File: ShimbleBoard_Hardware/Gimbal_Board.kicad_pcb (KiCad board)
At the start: 2 copper layers, 85 parts, among them Q1 Q_NMOS_GDS, Q2 Q_NMOS_GDS, Q3 Q_NMOS_GDS, Q4 Q_NMOS_GDS, Q5 Q_NMOS_GDS, Q6 Q_NMOS_GDS, Q7 Q_NMOS_GDS, Q8 Q_NMOS_GDS, SW1 SW_Push, SW10 SW_SPDT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

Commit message: All Connected I Believe
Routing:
- net GND: track 179.1 -> 169.7 mm
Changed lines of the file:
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@@
     (thickness 1.6)
     (drawings 1)
-    (tracks 403)
+    (tracks 401)
     (zones 0)
     (modules 85)
@@
   (segment (start 112.903 63.627) (end 113.03 63.5) (width 0.381) (layer F.Cu) (net 2))
   (segment (start 112.903 70.612) (end 112.903 63.627) (width 0.381) (layer F.Cu) (net 2))
-  (segment (start 149.916 77.526) (end 142.24 77.526) (width 0.381) (layer F.Cu) (net 2))
-  (segment (start 151.13 78.74) (end 149.916 77.526) (width 0.381) (layer F.Cu) (net 2))
   (segment (start 142.24 77.526) (end 141.10863 77.526) (width 0.381) (layer B.Cu) (net 2))
   (segment (start 119.634 77.526) (end 119.38 77.78) (width 0.381) (layer B.Cu) (net 2))

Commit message: All Connected I Believe
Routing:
- net Net-(D9-Pad2): track 0.00 -> 1.55 mm
- net Net-(D11-Pad2): track 0.00 -> 1.55 mm
- net Net-(D10-Pad2): track 0.00 -> 1.55 mm
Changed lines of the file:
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@@
     (thickness 1.6)
     (drawings 1)
-    (tracks 401)
+    (tracks 404)
     (zones 0)
     (modules 85)
@@
   (segment (start 162.052 66.576) (end 162.842 65.786) (width 0.381) (layer F.Cu) (net 29))
   (segment (start 162.052 67.31) (end 162.052 66.576) (width 0.381) (layer F.Cu) (net 29))
+  (segment (start 113.27 90.551) (end 114.822 90.551) (width 0.381) (layer F.Cu) (net 30))
+  (segment (start 121.567 90.551) (end 120.015 90.551) (width 0.381) (layer F.Cu) (net 31))
+  (segment (start 128.298 90.551) (end 126.746 90.551) (width 0.381) (layer F.Cu) (net 85))
   (segment (start 135.029 90.551) (end 133.477 90.551) (width 0.381) (layer F.Cu) (net 86))
   (segment (start 140.208 90.551) (end 141.76 90.551) (width 0.381) (layer F.Cu) (net 87))

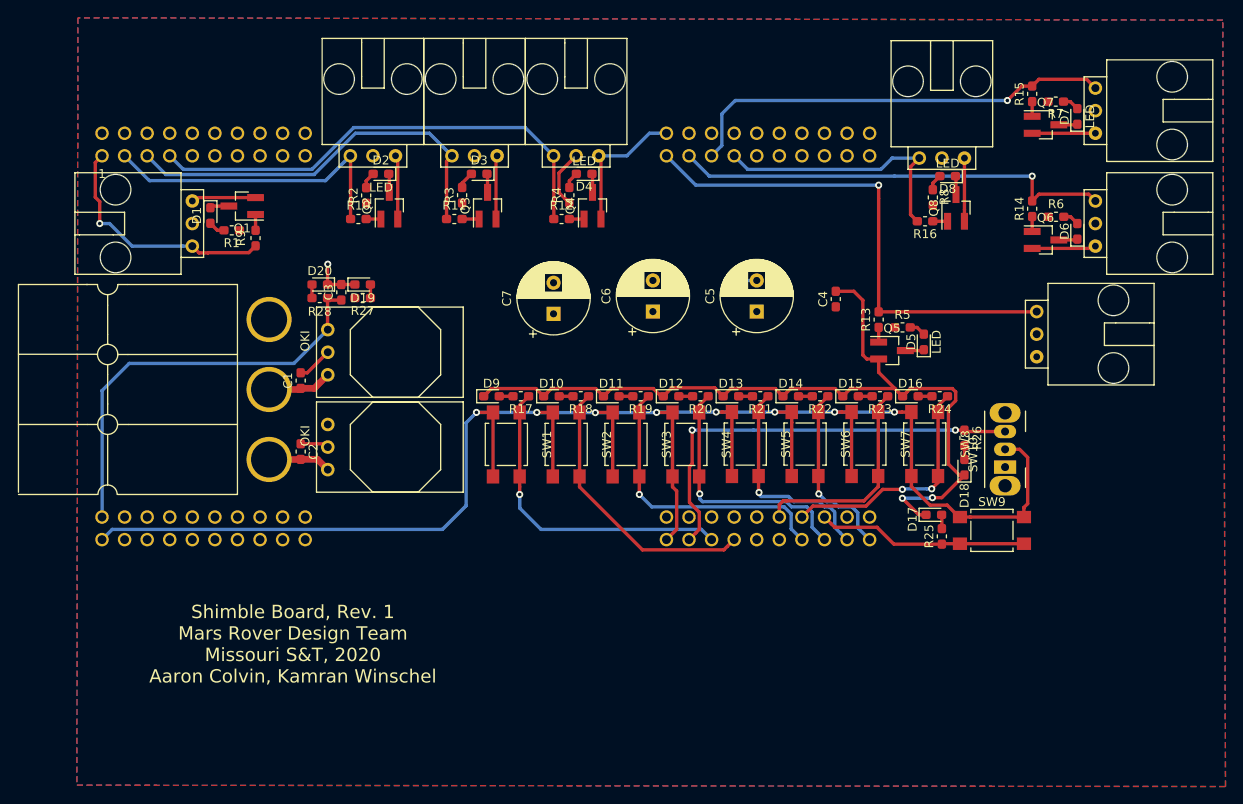
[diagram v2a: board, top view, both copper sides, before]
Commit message: Moved Labels
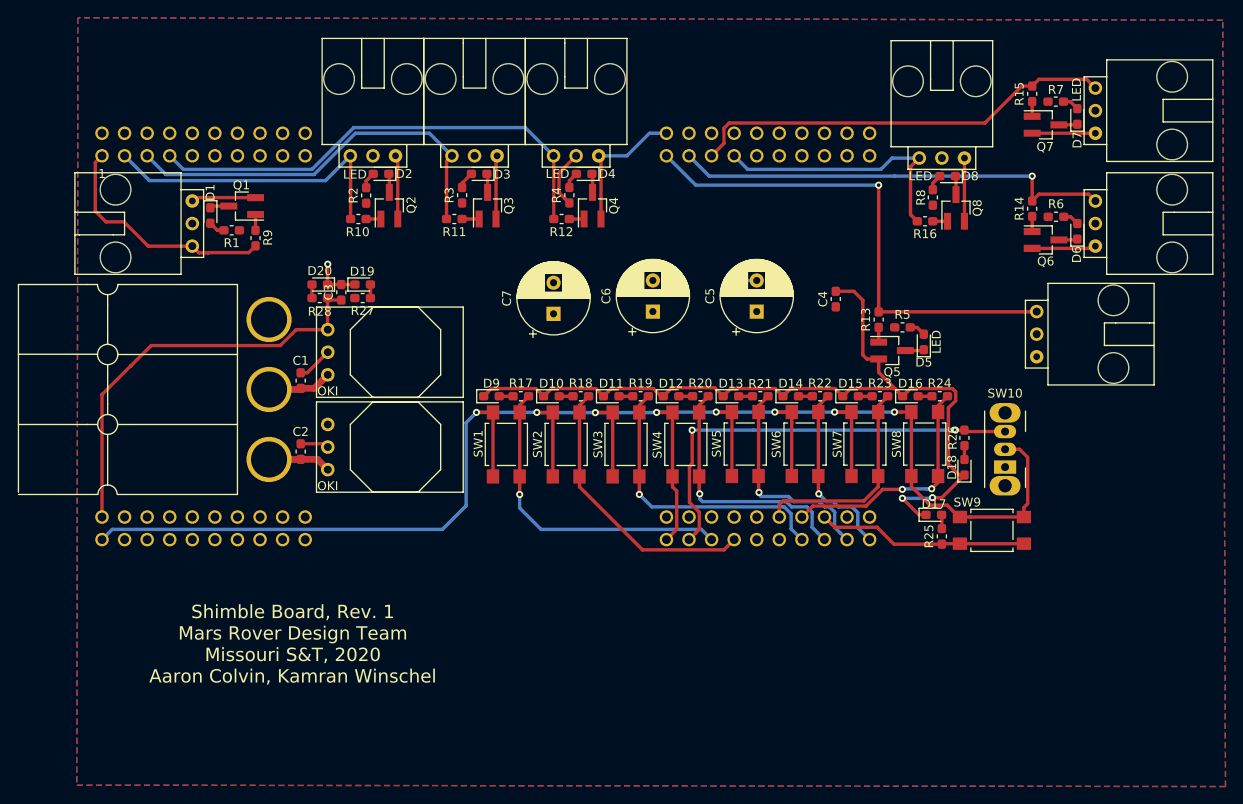
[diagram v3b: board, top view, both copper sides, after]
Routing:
- net Servo_Ctrl_7: track 49.2 -> 48.2 mm, vias 1 -> 0
- net Servo_Ctrl_1: track 27.4 -> 26.8 mm, vias 1 -> 0

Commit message: Cleaned
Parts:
- moved Q5 10.5 mm to (168.0, 85.3)
- moved R13 10.5 mm to (166.5, 81.9)
- moved D5 10.5 mm to (171.6, 84.4)
- moved R5 10.5 mm to (169.2, 82.7)
- moved C4 1.48 mm to (149.7, 79.4)
- moved C6 0.77 mm to (131.3, 81.2)
- moved C7 0.77 mm to (120.1, 81.4)
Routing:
- net GND: track 169.7 -> 167.0 mm
- net Servo_Ctrl_5: track 57.3 -> 55.3 mm, vias 1 -> 0
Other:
- board text added: "Servo Controls:"
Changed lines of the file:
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@@
   (general
     (thickness 1.6)
-    (drawings 1)
-    (tracks 403)
+    (drawings 2)
+    (tracks 409)
     (zones 0)
     (modules 85)
@@
   )
   (module Package_TO_SOT_SMD:SOT-23_Handsoldering (layer F.Cu)
-    (at 157.456 85.41)
+    (at 167.997 85.3465)
     (descr "SOT-23, Handsoldering")
     (tags SOT-23)
@@
   )
   (module Capacitor_THT:CP_Radial_D8.0mm_P3.50mm (layer F.Cu)
-    (at 130.556 81.026 90)
+    (at 131.318 81.153 90)
     (descr "CP, Radial series, Radial, pin pitch=3.50mm, , diameter=8mm, Electrolytic Capacitor")
     (tags "CP Radial series Radial pin pitch 3.50mm  diameter 8mm Electrolytic Capacitor")
@@
   )
   (module Capacitor_SMD:C_0603_1608Metric_Pad1.05x0.95mm_HandSolder (layer F.Cu)
-    (at 151.13 79.615 90)
+    (at 149.6695 79.361 90)
     (descr "Capacitor SMD 0603 (1608 Metric), square (rectangular) end terminal, IPC_7351 nominal with elongated pad for handsoldering. (Body size source: http://www.tortai-tech.com/upload/download/2011102023233369053.pdf), generated with kicad-footprint-generator")
     (tags "capacitor handsolder")
@@
   )
   (module Diode_SMD:D_0603_1608Metric_Pad1.05x0.95mm_HandSolder (layer F.Cu)
-    (at 161.036 84.441 90)
+    (at 171.577 84.3775 90)
     (descr "Diode SMD 0603 (1608 Metric), square (rectangular) end terminal, IPC_7351 nominal, (Body size source: http://www.tortai-tech.com/upload/download/2011102023233369053.pdf), generated with kicad-footprint-generator")
     (tags "diode handsolder")
     (attr smd)
-    (fp_text reference D5 (at -2.3 0 180) (layer F.SilkS)
+    (fp_text reference D5 (at -2.5794 -0.0254 270) (layer F.SilkS)
       (effects (font (size 1 1) (thickness 0.15)))
     )
-    (fp_text value LED (at 0 1.43 90) (layer F.SilkS)
+    (fp_text value LED (at 2.9705 0.0635 90) (layer F.SilkS)
       (effects (font (size 1 1) (thickness 0.15)))
     )
@@
   )
   (module Resistor_SMD:R_0603_1608Metric_Pad1.05x0.95mm_HandSolder (layer F.Cu)
-    (at 158.637 82.804)
+    (at 169.178 82.7405)
     (descr "Resistor SMD 0603 (1608 Metric), square (rectangular) end terminal, IPC_7351 nominal with elongated pad for handsoldering. (Body size source: http://www.tortai-tech.com/upload/download/2011102023233369053.pdf), generated with kicad-footprint-generator")
     (tags "resistor handsolder")
@@
   )
   (module Resistor_SMD:R_0603_1608Metric_Pad1.05x0.95mm_HandSolder (layer F.Cu)
-    (at 155.956 81.929 90)
+    (at 166.497 81.8655 90)
     (descr "Resistor SMD 0603 (1608 Metric), square (rectangular) end terminal, IPC_7351 nominal with elongated pad for handsoldering. (Body size source: http://www.tortai-tech.com/upload/download/2011102023233369053.pdf), generated with kicad-footprint-generator")
     (tags "resistor handsolder")
@@
   )
   (module Capacitor_THT:CP_Radial_D8.0mm_P3.50mm (layer F.Cu)
-    (at 119.38 81.28 90)
+    (at 120.142 81.407 90)
     (descr "CP, Radial series, Radial, pin pitch=3.50mm, , diameter=8mm, Electrolytic Capacitor")
     (tags "CP Radial series Radial pin pitch 3.50mm  diameter 8mm Electrolytic Capacitor")
@@
     )
   )
+  (gr_text "Servo Controls:" (at 119.126 86.614) (layer F.SilkS)
+    (effects (font (size 1.5 1.5) (thickness 0.3)))
+  )
   (gr_text "Shimble Board, Rev. 1\nMars Rover Design Team\nMissouri S&T, 2020\nAaron Colvin, Kamran Winschel" (at 90.05316 118.43766) (layer F.SilkS)
     (effects (font (size 1.5 1.5) (thickness 0.3)))
@@
   (segment (start 112.903 70.612) (end 112.903 63.627) (width 0.381) (layer F.Cu) (net 2))
   (segment (start 142.24 77.526) (end 141.10863 77.526) (width 0.381) (layer B.Cu) (net 2))
-  (segment (start 119.634 77.526) (end 119.38 77.78) (width 0.381) (layer B.Cu) (net 2))
-  (segment (start 154.625 86.36) (end 154.178 85.913) (width 0.381) (layer F.Cu) (net 2))
-  (segment (start 155.956 86.36) (end 154.625 86.36) (width 0.381) (layer F.Cu) (net 2))
-  (segment (start 154.178 85.913) (end 154.178 79.756) (width 0.381) (layer F.Cu) (net 2))
-  (segment (start 153.162 78.74) (end 151.13 78.74) (width 0.381) (layer F.Cu) (net 2))
-  (segment (start 154.178 79.756) (end 153.162 78.74) (width 0.381) (layer F.Cu) (net 2))
+  (segment (start 120.396 77.653) (end 120.142 77.907) (width 0.381) (layer B.Cu) (net 2))
   (segment (start 124.714 63.754) (end 124.46 63.5) (width 0.381) (layer F.Cu) (net 2))
   (segment (start 124.714 70.612) (end 124.714 63.754) (width 0.381) (layer F.Cu) (net 2))
@@
   (segment (start 137.5055 89.5985) (end 132.6795 89.5985) (width 0.381) (layer F.Cu) (net 2))
   (segment (start 138.458 90.551) (end 137.5055 89.5985) (width 0.381) (layer F.Cu) (net 2))
-  (segment (start 155.956 87.856) (end 157.78549 89.68549) (width 0.381) (layer F.Cu) (net 2))
-  (segment (start 155.956 86.36) (end 155.956 87.856) (width 0.381) (layer F.Cu) (net 2))
   (segment (start 159.150072 90.051928) (end 158.651 90.551) (width 0.381) (layer F.Cu) (net 2))
   (segment (start 159.51651 89.68549) (end 159.150072 90.051928) (width 0.381) (layer F.Cu) (net 2))
@@
   (segment (start 162.00845 101.961513) (end 163.059487 101.961513) (width 0.381) (layer F.Cu) (net 2))
   (via (at 93.98 75.692) (size 0.8) (drill 0.4) (layers F.Cu B.Cu) (net 2))
+  (segment (start 164.250632 87.211868) (end 164.250632 89.68549) (width 0.381) (layer F.Cu) (net 2))
+  (segment (start 165.166 86.2965) (end 164.250632 87.211868) (width 0.381) (layer F.Cu) (net 2))
+  (segment (start 166.497 86.2965) (end 165.166 86.2965) (width 0.381) (layer F.Cu) (net 2))
+  (segment (start 149.170428 77.986928) (end 149.106928 77.986928) (width 0.381) (layer F.Cu) (net 2))
+  (segment (start 149.6695 78.486) (end 149.170428 77.986928) (width 0.381) (layer F.Cu) (net 2))
+  (segment (start 148.646 77.526) (end 142.24 77.526) (width 0.381) (layer F.Cu) (net 2))
+  (segment (start 149.106928 77.986928) (end 148.646 77.526) (width 0.381) (layer F.Cu) (net 2))
   (segment (start 90.918 97.663) (end 90.932 97.649) (width 0.762) (layer F.Cu) (net 3))
   (segment (start 87.376 97.663) (end 90.918 97.663) (width 0.762) (layer F.Cu) (net 3))
@@
   (segment (start 119.408 63.528) (end 119.38 63.5) (width 0.381) (layer F.Cu) (net 9))
   (segment (start 119.408 70.612) (end 119.408 63.528) (width 0.381) (layer F.Cu) (net 9))
-  (segment (start 155.956 81.054) (end 155.956 68.326) (width 0.381) (layer F.Cu) (net 10))
-  (segment (start 155.956 68.326) (end 155.956 66.802) (width 0.381) (layer F.Cu) (net 10))
-  (via (at 155.956 66.802) (size 0.8) (drill 0.4) (layers F.Cu B.Cu) (net 10))
-  (segment (start 155.956 66.802) (end 135.382 66.802) (width 0.381) (layer B.Cu) (net 10))
-  (segment (start 135.382 66.802) (end 132.08 63.5) (width 0.381) (layer B.Cu) (net 10))
   (segment (start 173.708 81.054) (end 173.736 81.026) (width 0.381) (layer F.Cu) (net 10))
-  (segment (start 155.956 81.054) (end 173.708 81.054) (width 0.381) (layer F.Cu) (net 10))
+  (segment (start 173.7005 80.9905) (end 173.736 81.026) (width 0.381) (layer F.Cu) (net 10))
+  (segment (start 166.497 80.9905) (end 173.7005 80.9905) (width 0.381) (layer F.Cu) (net 10))
+  (segment (start 166.497 80.9905) (end 166.497 73.5965) (width 0.381) (layer F.Cu) (net 10))
+  (segment (start 166.497 73.5965) (end 165.316502 72.416002) (width 0.381) (layer F.Cu) (net 10))
+  (segment (start 165.316502 72.416002) (end 165.2905 72.416002) (width 0.381) (layer F.Cu) (net 10))
+  (segment (start 165.2905 72.39) (end 165.316502 72.416002) (width 0.381) (layer F.Cu) (net 10))
+  (segment (start 132.08 63.5) (end 134.874 66.294) (width 0.381) (layer F.Cu) (net 10))
+  (segment (start 157.6705 66.294) (end 158.958991 67.582491) (width 0.381) (layer F.Cu) (net 10))
+  (segment (start 158.958991 67.582491) (end 158.958991 70.936133) (width 0.381) (layer F.Cu) (net 10))
+  (segment (start 158.958991 70.936133) (end 160.412858 72.39) (width 0.381) (layer F.Cu) (net 10))
+  (segment (start 134.874 66.294) (end 157.6705 66.294) (width 0.381) (layer F.Cu) (net 10))
+  (segment (start 160.412858 72.39) (end 165.2905 72.39) (width 0.381) (layer F.Cu) (net 10))
   (segment (start 173.228 68.58) (end 173.99 67.818) (width 0.381) (layer F.Cu) (net 11))
   (segment (start 179.578001 67.818001) (end 180.34 68.58) (width 0.381) (layer F.Cu) (net 11))
@@
   (segment (start 121.158 66.322) (end 121.948 65.532) (width 0.381) (layer F.Cu) (net 21))
   (segment (start 121.158 67.056) (end 121.158 66.322) (width 0.381) (layer F.Cu) (net 21))
-  (segment (start 160.942 85.41) (end 161.036 85.316) (width 0.381) (layer F.Cu) (net 22))
-  (segment (start 158.956 85.41) (end 160.942 85.41) (width 0.381) (layer F.Cu) (net 22))
-  (segment (start 160.274 82.804) (end 161.036 83.566) (width 0.381) (layer F.Cu) (net 23))
-  (segment (start 159.512 82.804) (end 160.274 82.804) (width 0.381) (layer F.Cu) (net 23))
+  (segment (start 171.483 85.3465) (end 171.577 85.2525) (width 0.381) (layer F.Cu) (net 22))
+  (segment (start 169.497 85.3465) (end 171.483 85.3465) (width 0.381) (layer F.Cu) (net 22))
+  (segment (start 170.815 82.7405) (end 171.577 83.5025) (width 0.381) (layer F.Cu) (net 23))
+  (segment (start 170.053 82.7405) (end 170.815 82.7405) (width 0.381) (layer F.Cu) (net 23))
   (segment (start 177.546 70.358) (end 178.308 71.12) (width 0.381) (layer F.Cu) (net 24))
   (segment (start 176.784 70.358) (end 177.546 70.358) (width 0.381) (layer F.Cu) (net 24))
@@
   (segment (start 111.003 70.612) (end 109.093 70.612) (width 0.381) (layer F.Cu) (net 109))
   (segment (start 122.814 70.612) (end 121.158 70.612) (width 0.381) (layer F.Cu) (net 110))
-  (segment (start 155.956 84.46) (end 155.956 82.804) (width 0.381) (layer F.Cu) (net 111))
+  (segment (start 166.497 84.3965) (end 166.497 82.7405) (width 0.381) (layer F.Cu) (net 111))
   (segment (start 173.228 72.014) (end 173.228 70.33) (width 0.381) (layer F.Cu) (net 112))
   (segment (start 173.228 57.404) (end 173.228 59.06) (width 0.381) (layer F.Cu) (net 113))

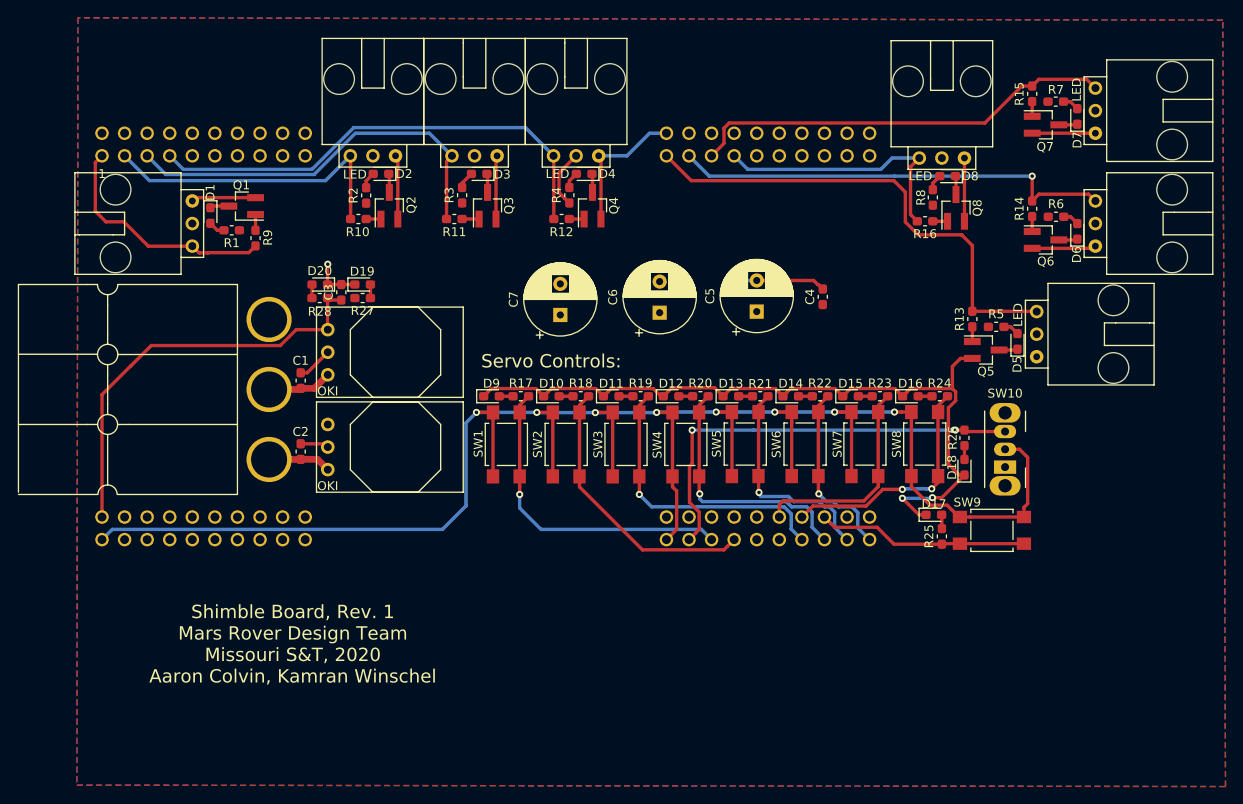
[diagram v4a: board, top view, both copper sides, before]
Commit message: Added border that needs fixing
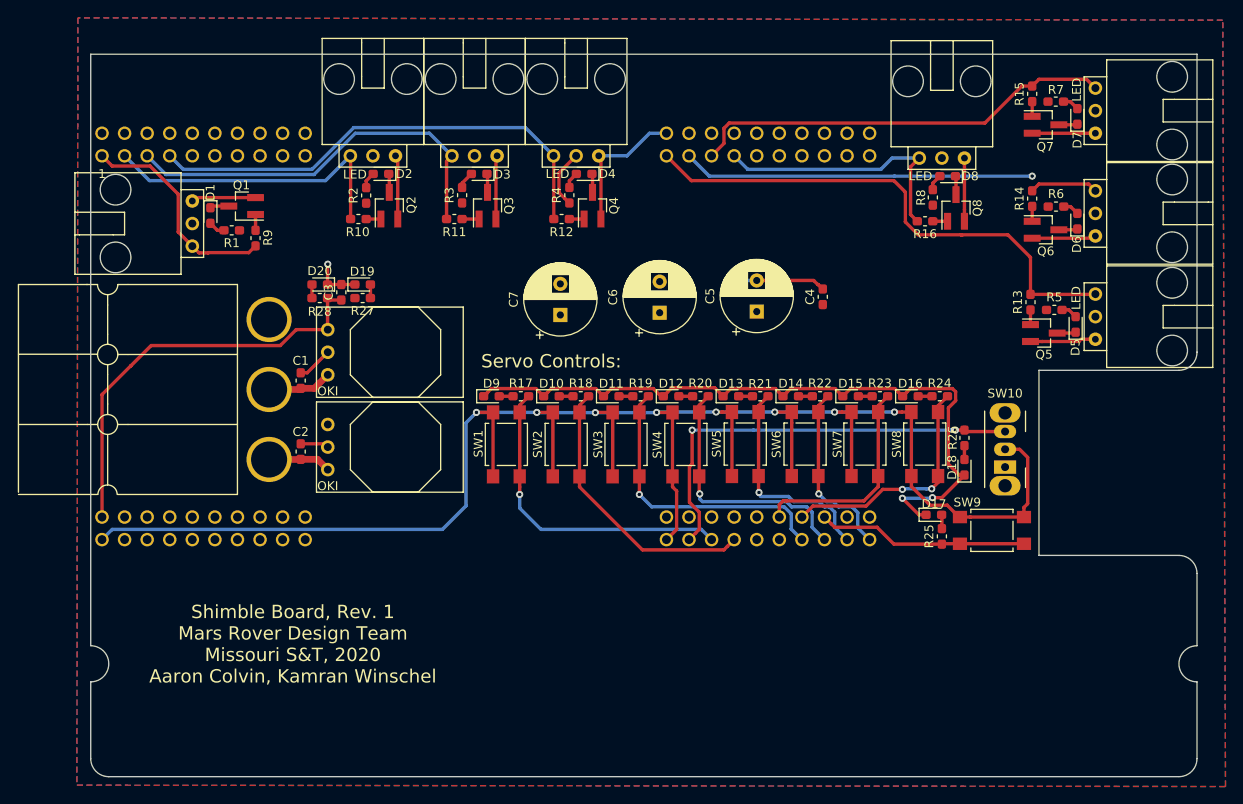
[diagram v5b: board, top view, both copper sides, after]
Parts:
- moved Conn5 6.89 mm to (180.3, 81.6)
- moved D5 6.81 mm to (178.1, 82.5)
- moved R5 6.81 mm to (175.7, 80.8)
- moved Q5 6.81 mm to (174.5, 83.4)
- moved R13 6.81 mm to (173.0, 80.0)
- moved Conn6 1.14 mm to (180.3, 70.0)
- moved D6 1.14 mm to (178.3, 70.9)
- moved Q6 1.14 mm to (174.7, 71.8)
- moved R14 1.14 mm to (173.2, 68.3)
- moved R6 1.14 mm to (175.9, 69.2)
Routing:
- net Servo_Ctrl_5: track 55.3 -> 59.3 mm
- net Servo_Ctrl_6: track 50.1 -> 47.3 mm
- net GND: track 167.0 -> 169.3 mm
- net Servo_Ctrl_1: track 26.8 -> 24.6 mm
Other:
- board outline added: 124.5 x 81.3 mm
